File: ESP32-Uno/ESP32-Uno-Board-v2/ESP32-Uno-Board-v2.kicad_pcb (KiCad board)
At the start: 2 copper layers, 68.8 x 53.2 mm, 19 parts, among them J1 USB-C_Receptacle_Data_16P_GCT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, J2 Barrel_Jack_Switch, Q1 DMP6180SK3, SW1 SW_SPDT, SW2 SW_Push_SMD_6x3.5, U1 ESP32-S3-WROOM-1, U2 LM1117MP-3.3, U3 AMS1117-5V

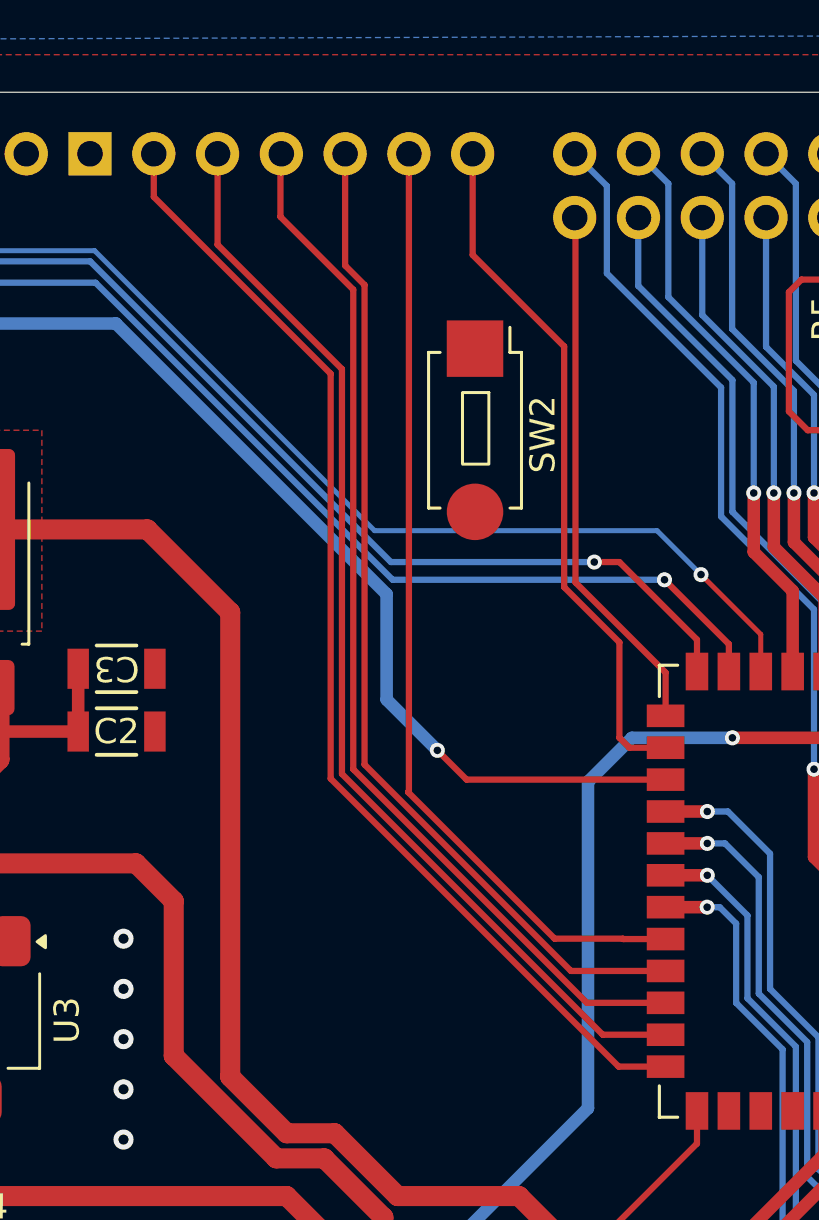
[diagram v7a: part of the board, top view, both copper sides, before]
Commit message: ESP32-Uno
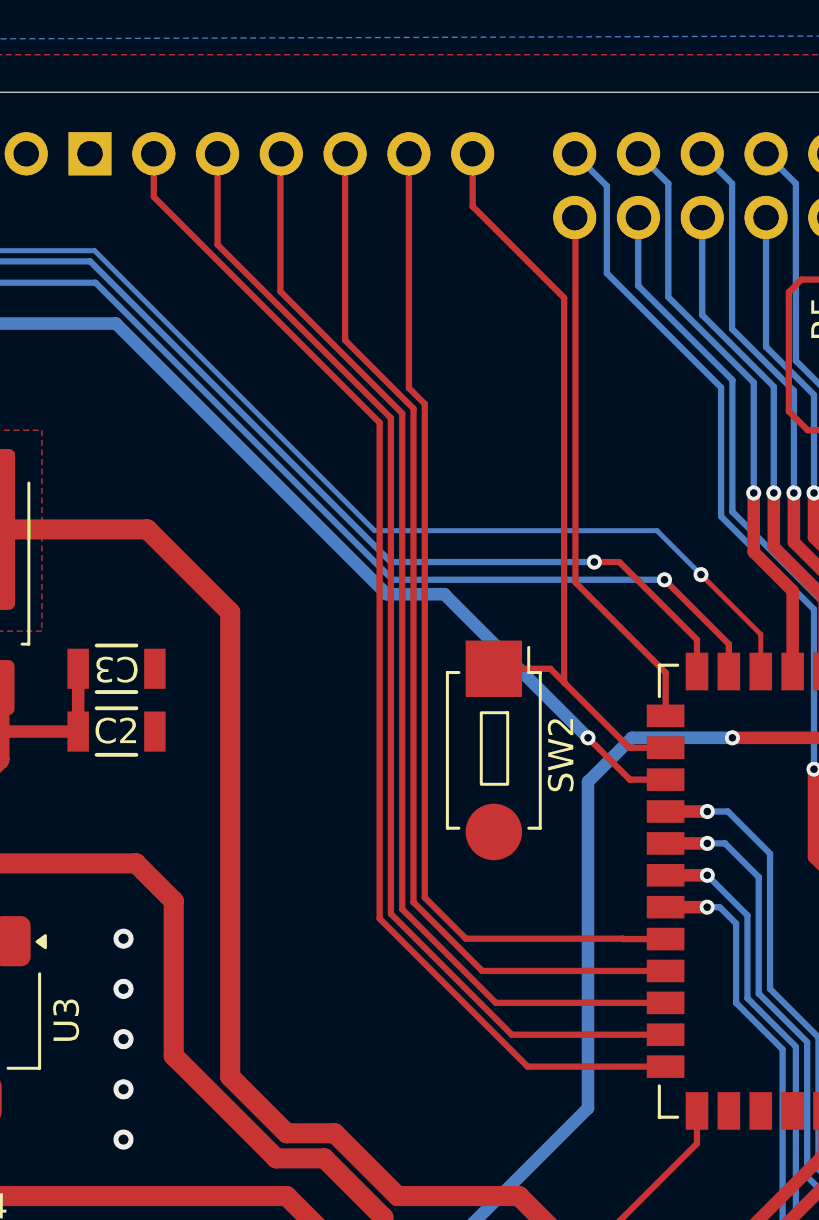
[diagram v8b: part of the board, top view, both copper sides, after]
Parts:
- moved SW2 12.8 mm to (152.5, 122.5)
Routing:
- net /GPIO46: track 27.7 -> 30.7 mm
- net /SCL: track 46.3 -> 43.9 mm
- net /GPIO48: track 43.9 -> 46.1 mm
- net /GPIO47: track 42.0 -> 44.1 mm
- net /GPIO45: track 45.9 -> 48.0 mm
- net /GPIO21: track 40.0 -> 42.1 mm
- net /GPIO14: track 38.1 -> 40.2 mm
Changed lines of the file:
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@@
 	(footprint "Alexander Footprint Library:SW_PUSH_6x3.5mm"
 		(layer "F.Cu")
-		(at 151.75 109.75 -90)
+		(at 152.5 122.5 -90)
 		(descr "tactile push button, 6x3.5mm, https://www.apem.com/idec-apem/en_US/PCB-switches/Tactile-Switches/MJTP-6mm-through-hole/c/MJTP_6mm_through%20hole?page=1")
 		(tags "PHAP3362 6mm tact sw THT")
@@
 	)
 	(segment
-		(start 146.576 106.439604)
-		(end 146.576 101.99)
+		(start 159.34 134.535)
+		(end 152.035 134.535)
 		(width 0.25)
 		(layer "F.Cu")
@@
 	)
 	(segment
-		(start 147.35 107.213604)
-		(end 146.576 106.439604)
+		(start 152.035 134.535)
+		(end 149.3 131.8)
 		(width 0.25)
 		(layer "F.Cu")
@@
 	)
 	(segment
-		(start 147.35 126.315812)
-		(end 147.35 107.213604)
+		(start 146.576 109.416812)
+		(end 146.576 101.99)
 		(width 0.25)
 		(layer "F.Cu")
@@
 	)
 	(segment
-		(start 155.569188 134.535)
-		(end 147.35 126.315812)
+		(start 149.3 112.140812)
+		(end 146.576 109.416812)
 		(width 0.25)
 		(layer "F.Cu")
@@
 	)
 	(segment
-		(start 159.34 134.535)
-		(end 155.569188 134.535)
+		(start 149.3 131.8)
+		(end 149.3 112.140812)
 		(width 0.25)
 		(layer "F.Cu")
@@
 	)
 	(segment
-		(start 138.956 103.706)
-		(end 138.956 101.99)
+		(start 147.95 132.45)
+		(end 147.95 112.7)
 		(width 0.25)
 		(layer "F.Cu")
@@
 	)
 	(segment
-		(start 159.34 138.345)
-		(end 157.47 138.345)
+		(start 147.95 112.7)
+		(end 138.956 103.706)
 		(width 0.25)
 		(layer "F.Cu")
@@
 	)
 	(segment
-		(start 146 110.75)
-		(end 138.956 103.706)
+		(start 153.845 138.345)
+		(end 147.95 132.45)
 		(width 0.25)
 		(layer "F.Cu")
@@
 	)
 	(segment
-		(start 146 126.875)
-		(end 146 110.75)
+		(start 159.34 138.345)
+		(end 153.845 138.345)
 		(width 0.25)
 		(layer "F.Cu")
@@
 	)
 	(segment
-		(start 157.47 138.345)
-		(end 146 126.875)
+		(start 138.956 103.706)
+		(end 138.956 101.99)
 		(width 0.25)
 		(layer "F.Cu")
@@
 	)
 	(segment
-		(start 159.34 133.265)
-		(end 157.651396 133.265)
+		(start 149.75 111.954416)
+		(end 149.75 131.613604)
 		(width 0.25)
 		(layer "F.Cu")
@@
 	)
 	(segment
-		(start 149.085292 127.414708)
-		(end 149.116 127.384)
+		(start 149.116 101.99)
+		(end 149.116 111.320416)
 		(width 0.25)
 		(layer "F.Cu")
@@
 	)
 	(segment
-		(start 154.920584 133.25)
-		(end 149.085292 127.414708)
+		(start 157.636396 133.25)
+		(end 157.651396 133.265)
 		(width 0.25)
 		(layer "F.Cu")
@@
 	)
 	(segment
-		(start 149.116 127.384)
-		(end 149.116 101.99)
+		(start 149.116 111.320416)
+		(end 149.75 111.954416)
 		(width 0.25)
 		(layer "F.Cu")
@@
 	)
 	(segment
-		(start 157.636396 133.25)
-		(end 154.920584 133.25)
+		(start 149.75 131.613604)
+		(end 151.386396 133.25)
 		(width 0.25)
 		(layer "F.Cu")
@@
 	(segment
 		(start 157.651396 133.265)
-		(end 157.636396 133.25)
+		(end 159.34 133.265)
 		(width 0.25)
 		(layer "F.Cu")
@@
 	)
 	(segment
-		(start 159.34 137.075)
-		(end 156.836396 137.075)
+		(start 151.386396 133.25)
+		(end 157.636396 133.25)
 		(width 0.25)
 		(layer "F.Cu")
-		(net 19)
+		(net 18)
 	)
 	(segment
-		(start 156.836396 137.075)
-		(end 146.45 126.688604)
+		(start 148.4 132.263604)
+		(end 148.4 112.513604)
 		(width 0.25)
 		(layer "F.Cu")
@@
 	)
 	(segment
-		(start 146.45 126.688604)
-		(end 146.45 110.563604)
+		(start 148.4 112.513604)
+		(end 141.496 105.609604)
 		(width 0.25)
 		(layer "F.Cu")
@@
 	)
 	(segment
-		(start 146.45 110.563604)
-		(end 141.496 105.609604)
+		(start 159.34 137.075)
+		(end 153.211396 137.075)
 		(width 0.25)
 		(layer "F.Cu")
@@
 	)
 	(segment
+		(start 153.211396 137.075)
+		(end 148.4 132.263604)
+		(width 0.25)
+		(layer "F.Cu")
+		(net 19)
+	)
+	(segment
 		(start 161 128.185)
 		(end 159.34 128.185)
@@
 	)
 	(segment
-		(start 159.34 135.805)
-		(end 156.202792 135.805)
+		(start 144 102.026)
+		(end 144.036 101.99)
 		(width 0.25)
 		(layer "F.Cu")
@@
 	)
 	(segment
-		(start 144 102.026)
-		(end 144.036 101.99)
+		(start 159.34 135.805)
+		(end 152.577792 135.805)
 		(width 0.25)
 		(layer "F.Cu")
@@
 	)
 	(segment
-		(start 156.202792 135.805)
-		(end 146.9 126.502208)
+		(start 148.85 132.077208)
+		(end 148.85 112.327208)
 		(width 0.25)
 		(layer "F.Cu")
@@
 	)
 	(segment
-		(start 146.9 126.502208)
-		(end 146.9 107.4)
+		(start 144 107.477208)
+		(end 144 102.026)
 		(width 0.25)
 		(layer "F.Cu")
@@
 	)
 	(segment
-		(start 146.9 107.4)
-		(end 144 104.5)
+		(start 148.85 112.327208)
+		(end 144 107.477208)
 		(width 0.25)
 		(layer "F.Cu")
@@
 	)
 	(segment
-		(start 144 104.5)
-		(end 144 102.026)
+		(start 152.577792 135.805)
+		(end 148.85 132.077208)
 		(width 0.25)
 		(layer "F.Cu")
@@
 	)
 	(segment
-		(start 157.895 125.645)
-		(end 157.5 125.25)
+		(start 154.75 122.5)
+		(end 155.3 123.05)
 		(width 0.25)
 		(layer "F.Cu")
@@
 	)
 	(segment
-		(start 151.656 106.019604)
-		(end 151.656 101.99)
+		(start 157.895 125.645)
+		(end 155.3 123.05)
 		(width 0.25)
 		(layer "F.Cu")
@@
 	)
 	(segment
-		(start 157.5 125.25)
-		(end 157.5 121.448896)
+		(start 159.34 125.645)
+		(end 157.895 125.645)
 		(width 0.25)
 		(layer "F.Cu")
@@
 	)
 	(segment
-		(start 155.3 119.248896)
-		(end 155.3 109.663604)
+		(start 155.3 107.731802)
+		(end 151.656 104.087802)
 		(width 0.25)
 		(layer "F.Cu")
@@
 	)
 	(segment
-		(start 155.3 109.663604)
-		(end 151.656 106.019604)
+		(start 152.5 122.5)
+		(end 154.75 122.5)
 		(width 0.25)
 		(layer "F.Cu")
@@
 	)
 	(segment
-		(start 159.34 125.645)
-		(end 157.895 125.645)
+		(start 155.3 123.05)
+		(end 155.3 107.731802)
 		(width 0.25)
 		(layer "F.Cu")
@@
 	)
 	(segment
-		(start 157.5 121.448896)
-		(end 155.3 119.248896)
+		(start 151.656 104.087802)
+		(end 151.656 101.99)
 		(width 0.25)
 		(layer "F.Cu")
@@
 	)
 	(segment
-		(start 132 108.75)
-		(end 130.25 108.75)
-		(width 0.5)
+		(start 156.25 125.25)
+		(end 157.915 126.915)
+		(width 0.25)
 		(layer "F.Cu")
 		(net 50)
 	)
 	(segment
-		(start 150.25 125.75)
-		(end 151.415 126.915)
-		(width 0.25)
+		(start 132 108.75)
+		(end 130.25 108.75)
+		(width 0.5)
 		(layer "F.Cu")
 		(net 50)
@@
 	)
 	(segment
-		(start 151.415 126.915)
+		(start 157.915 126.915)
 		(end 159.34 126.915)
 		(width 0.25)
@@
 	)
 	(via
-		(at 150.25 125.75)
+		(at 156.25 125.25)
 		(size 0.6)
 		(drill 0.3)
@@
 	)
 	(segment
-		(start 148.229391 119.53)
-		(end 137.449391 108.75)
+		(start 150.53 119.53)
+		(end 148.229391 119.53)
 		(width 0.5)
 		(layer "B.Cu")
@@
 	)
 	(segment
-		(start 150.25 125.75)
-		(end 148.229391 123.729391)
+		(start 148.229391 119.53)
+		(end 137.449391 108.75)
 		(width 0.5)
 		(layer "B.Cu")
@@
 	)
 	(segment
-		(start 148.229391 123.729391)
-		(end 148.229391 119.53)
+		(start 156.25 125.25)
+		(end 150.53 119.53)
 		(width 0.5)
 		(layer "B.Cu")
